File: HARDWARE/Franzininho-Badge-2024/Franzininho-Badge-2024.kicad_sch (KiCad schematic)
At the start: 47 parts, among them J1 Conn_01x03_Pin, J2 Conn_01x04_Pin, Q1 SIL2308, SW1 ON/OFF, SW2 USER, SW3 RESET, U1 1.54in 200x200, U2 CH32V003F4P6, U3 2.13in 250x122, U4 OLED 128x64 1.3"

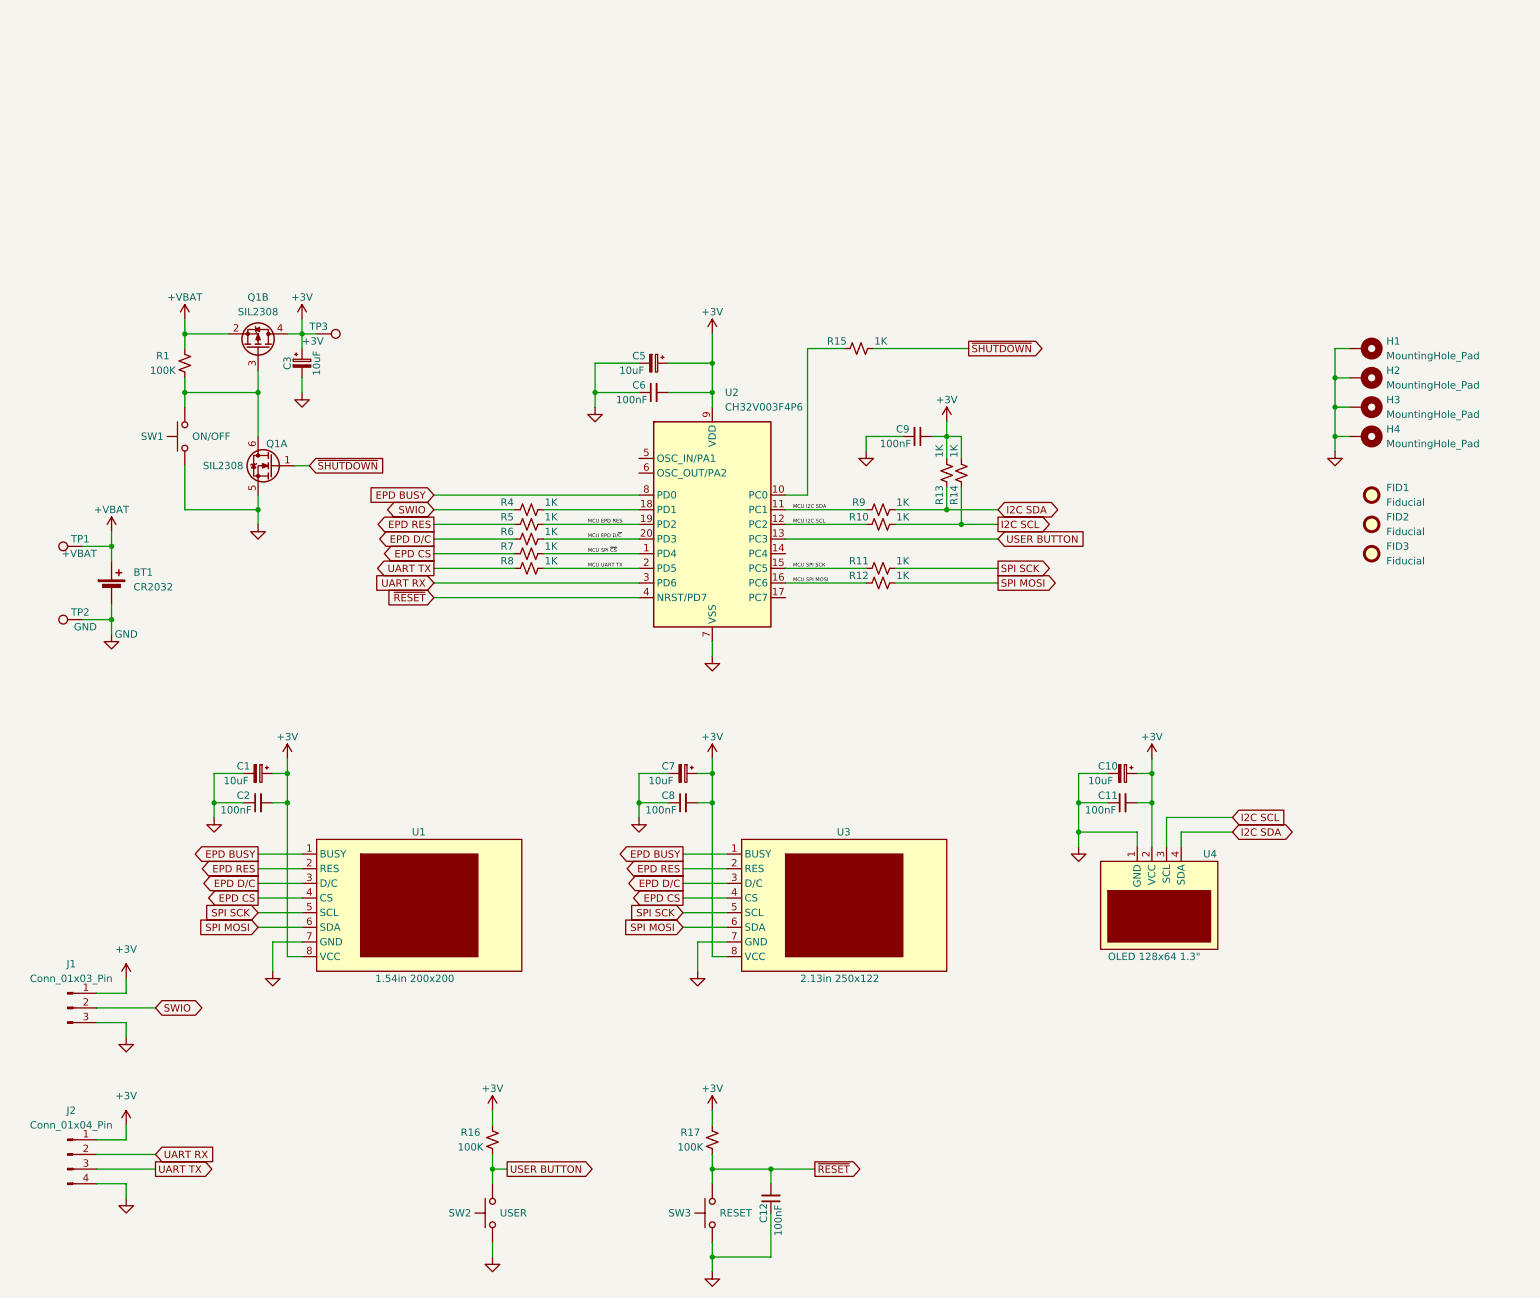
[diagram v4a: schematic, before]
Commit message: Finalização do projeto; adicionados test points e LEDs; adicionado conector para SPI; ajuste nas marcações; renumeração; ajustes no layout.
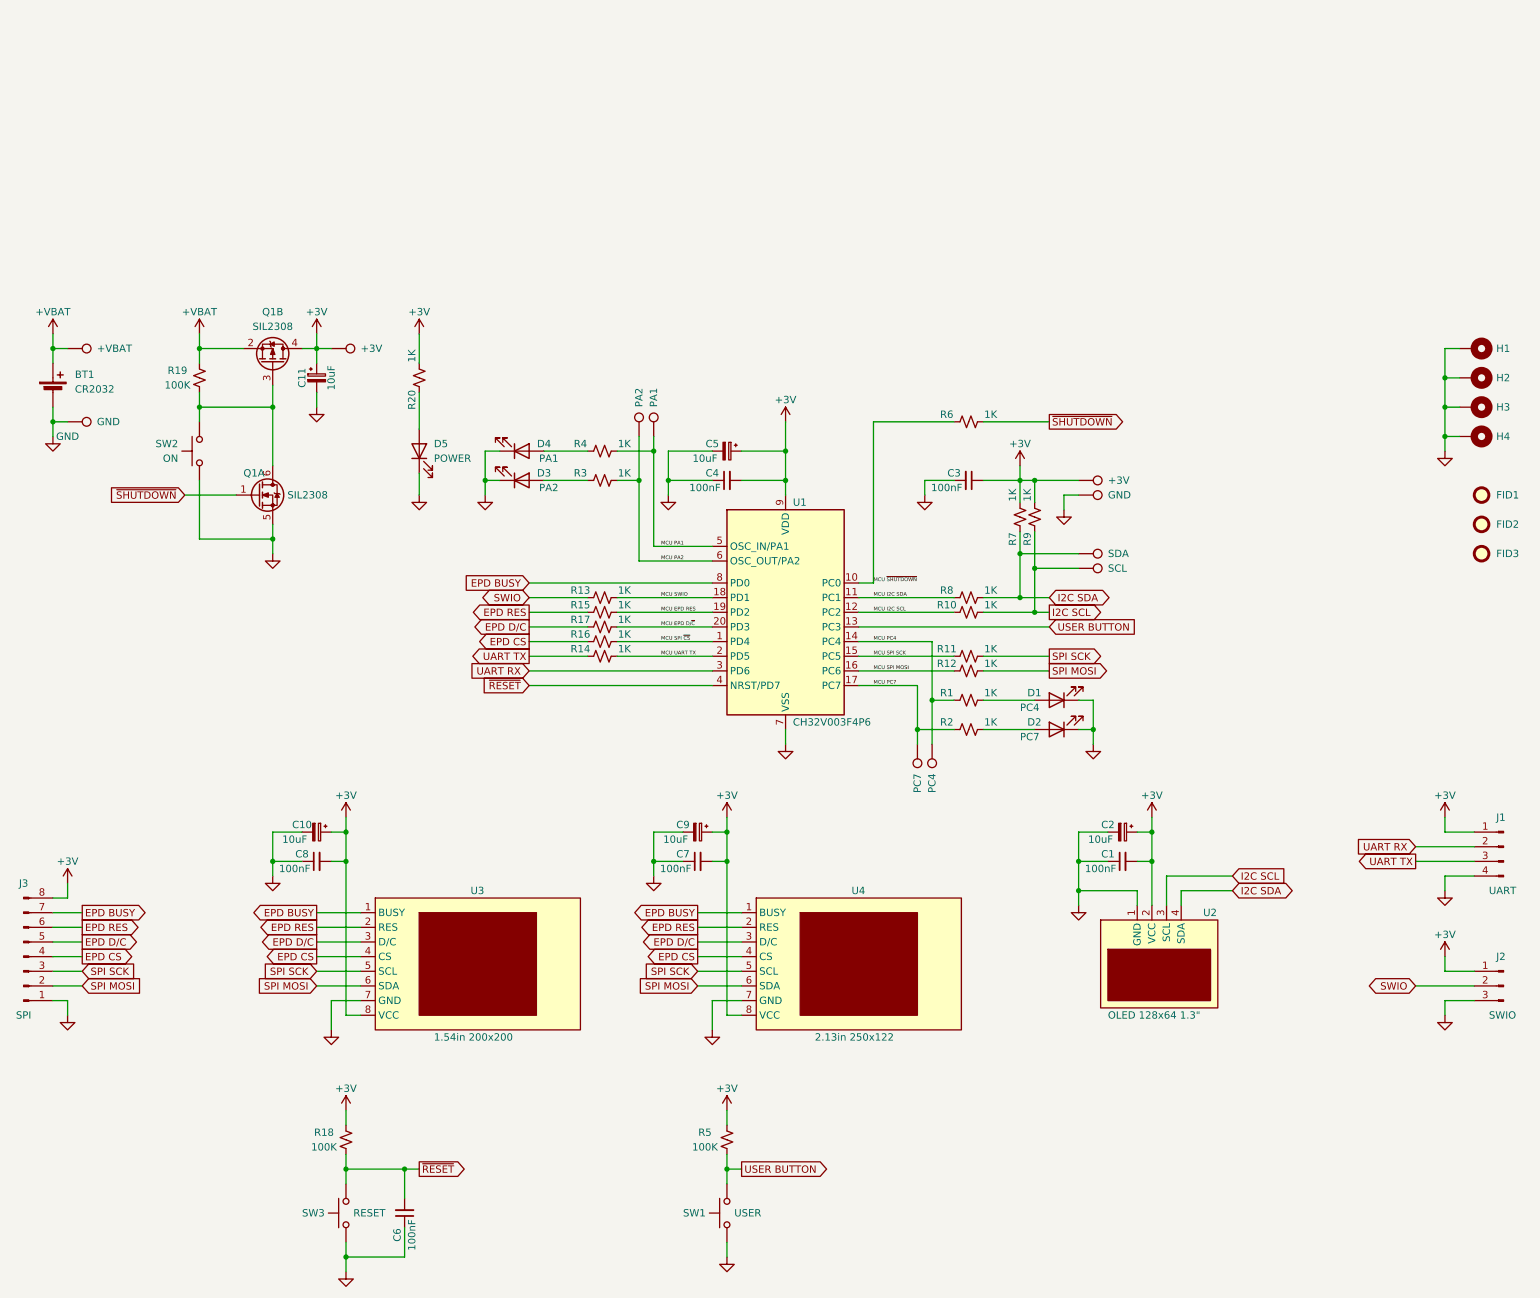
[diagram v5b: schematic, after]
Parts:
- added D1: PC4, LED_SMD:LED_0603_1608Metric_Pad1.05x0.95mm_HandSolder, symbol Device:LED
- added D2: PC7, LED_SMD:LED_0603_1608Metric_Pad1.05x0.95mm_HandSolder, symbol Device:LED
- added D3: PA2, LED_SMD:LED_0603_1608Metric_Pad1.05x0.95mm_HandSolder, symbol Device:LED
- added D4: PA1, LED_SMD:LED_0603_1608Metric_Pad1.05x0.95mm_HandSolder, symbol Device:LED
- added D5: POWER, LED_SMD:LED_0603_1608Metric_Pad1.05x0.95mm_HandSolder, symbol Device:LED
- added J3: SPI, Connector_PinHeader_2.54mm:PinHeader_1x08_P2.54mm_Horizontal, symbol Connector:Conn_01x08_Pin
- added R1, R2, R20, R3, R4: 1K, Resistor_SMD:R_0603_1608Metric_Pad0.98x0.95mm_HandSolder, symbol Device:R_Small_US
- added TP1: SDA, TestPoint:TestPoint_THTPad_D1.5mm_Drill0.7mm, symbol Connector:TestPoint
- added TP2: SCL, TestPoint:TestPoint_THTPad_D1.5mm_Drill0.7mm, symbol Connector:TestPoint
- added TP3: +3V, TestPoint:TestPoint_THTPad_D1.5mm_Drill0.7mm, symbol Connector:TestPoint
- added TP4: GND, TestPoint:TestPoint_THTPad_D1.5mm_Drill0.7mm, symbol Connector:TestPoint
- added TP5: PC4, TestPoint:TestPoint_THTPad_D1.5mm_Drill0.7mm, symbol Connector:TestPoint
- added TP6: PC7, TestPoint:TestPoint_THTPad_D1.5mm_Drill0.7mm, symbol Connector:TestPoint
- added TP7: PA2, TestPoint:TestPoint_THTPad_D1.5mm_Drill0.7mm, symbol Connector:TestPoint
- added TP8: PA1, TestPoint:TestPoint_THTPad_D1.5mm_Drill0.7mm, symbol Connector:TestPoint
- J1: renamed from J2; value Conn_01x04_Pin -> UART
- J2: renamed from J1; value Conn_01x03_Pin -> SWIO
- SW2: renamed from SW1; value ON/OFF -> ON
- renumbered C11 to C1, C1 to C10, C3 to C11, C10 to C2, C9 to C3, C6 to C4, C12 to C6, C8 to C7, C2 to C8, C7 to C9, R4 to R13, R8 to R14, R5 to R15, R7 to R16, R6 to R17, R17 to R18, R1 to R19, R16 to R5, R15 to R6, R13 to R7, R9 to R8, R14 to R9, SW2 to SW1, TP1 to TP10, TP3 to TP11, TP2 to TP9, U2 to U1, U4 to U2, U1 to U3, U3 to U4
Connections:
- net +3V: now also J3.8 (Pin_8), R20.2, TP3.1
- net EPD BUSY: now also J3.7 (Pin_7)
- net EPD CS: now also J3.4 (Pin_4)
- net EPD D/C: now also J3.5 (Pin_5)
- net EPD RES: now also J3.6 (Pin_6)
- net GND: now also D1.1 (K), D2.1 (K), D3.1 (K), D4.1 (K), D5.1 (K), J3.1 (Pin_1), TP4.1
- net I2C SCL: now also TP2.1
- net I2C SDA: now also TP1.1
- net SPI MOSI: now also J3.2 (Pin_2)
- net SPI SCK: now also J3.3 (Pin_3)
- net MCU SWIO: now reaches R13.2, U1.18 (PD1)
- net MCU ~{SHUTDOWN}: now reaches R6.1, U1.10 (PC0)
- net MCU PC4: now reaches U1.14 (PC4)
- net MCU PC4: now also R1.1, TP5.1
- net MCU PC7: now reaches U1.17 (PC7)
- net MCU PC7: now also R2.1, TP6.1
- net MCU PA1: now reaches U1.5 (OSC_IN/PA1)
- net MCU PA1: now also R4.2, TP8.1
- net MCU PA2: now reaches U1.6 (OSC_OUT/PA2)
- net MCU PA2: now also R3.2, TP7.1
- new net: D1.2 (A), R1.2
- new net: D2.2 (A), R2.2
- new net: D5.2 (A), R20.1
- new net: D4.2 (A), R4.1
- new net: D3.2 (A), R3.1
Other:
- company: (none) -> Eng. André A. M. Araújo
- moved on the sheet: BT1, C1, C10, C11, C2, C3, C4, C5, C6, C7, C8, C9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

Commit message: Finalização do esquemático e layout.
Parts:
- U3: value 1.54in 200x200 -> EPD 200x200 1.54"
- U4: value 2.13in 250x122 -> EPD 250x122 2.13"
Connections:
- net LED PC4: now reaches D1.2 (A), R1.2
- net LED PC7: now reaches D2.2 (A), R2.2
- net LED POWER: now reaches D5.2 (A), R20.1
- net SWITCH ~{ON}: now reaches Q1.3 (G2), Q1.6 (D1), R19.1, SW2.2
- net LED PA1: now reaches D4.2 (A), R4.1
- net LED PA2: now reaches D3.2 (A), R3.1
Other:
- moved on the sheet: D1, D2, D3, D4, D5, R20

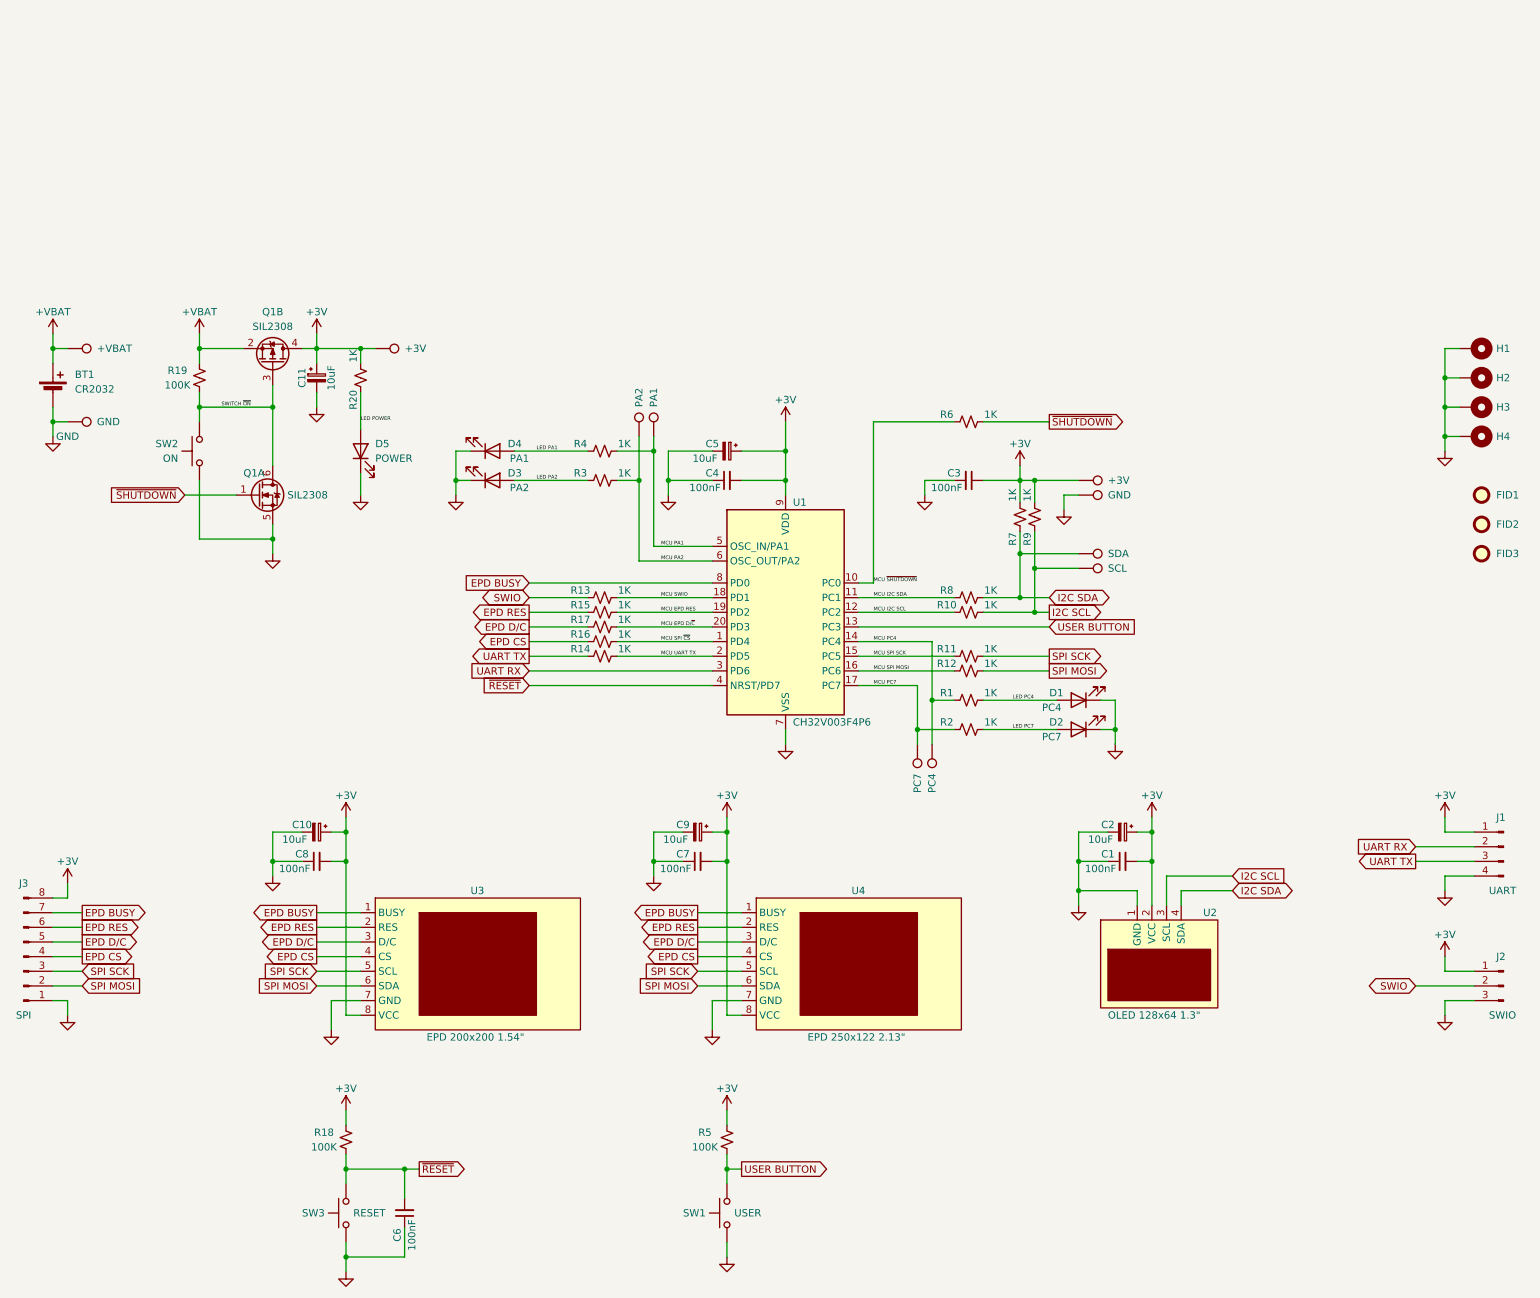
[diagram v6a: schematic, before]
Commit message: Revisão de valores dos resistores. Geração de novo PDF do esquemático.
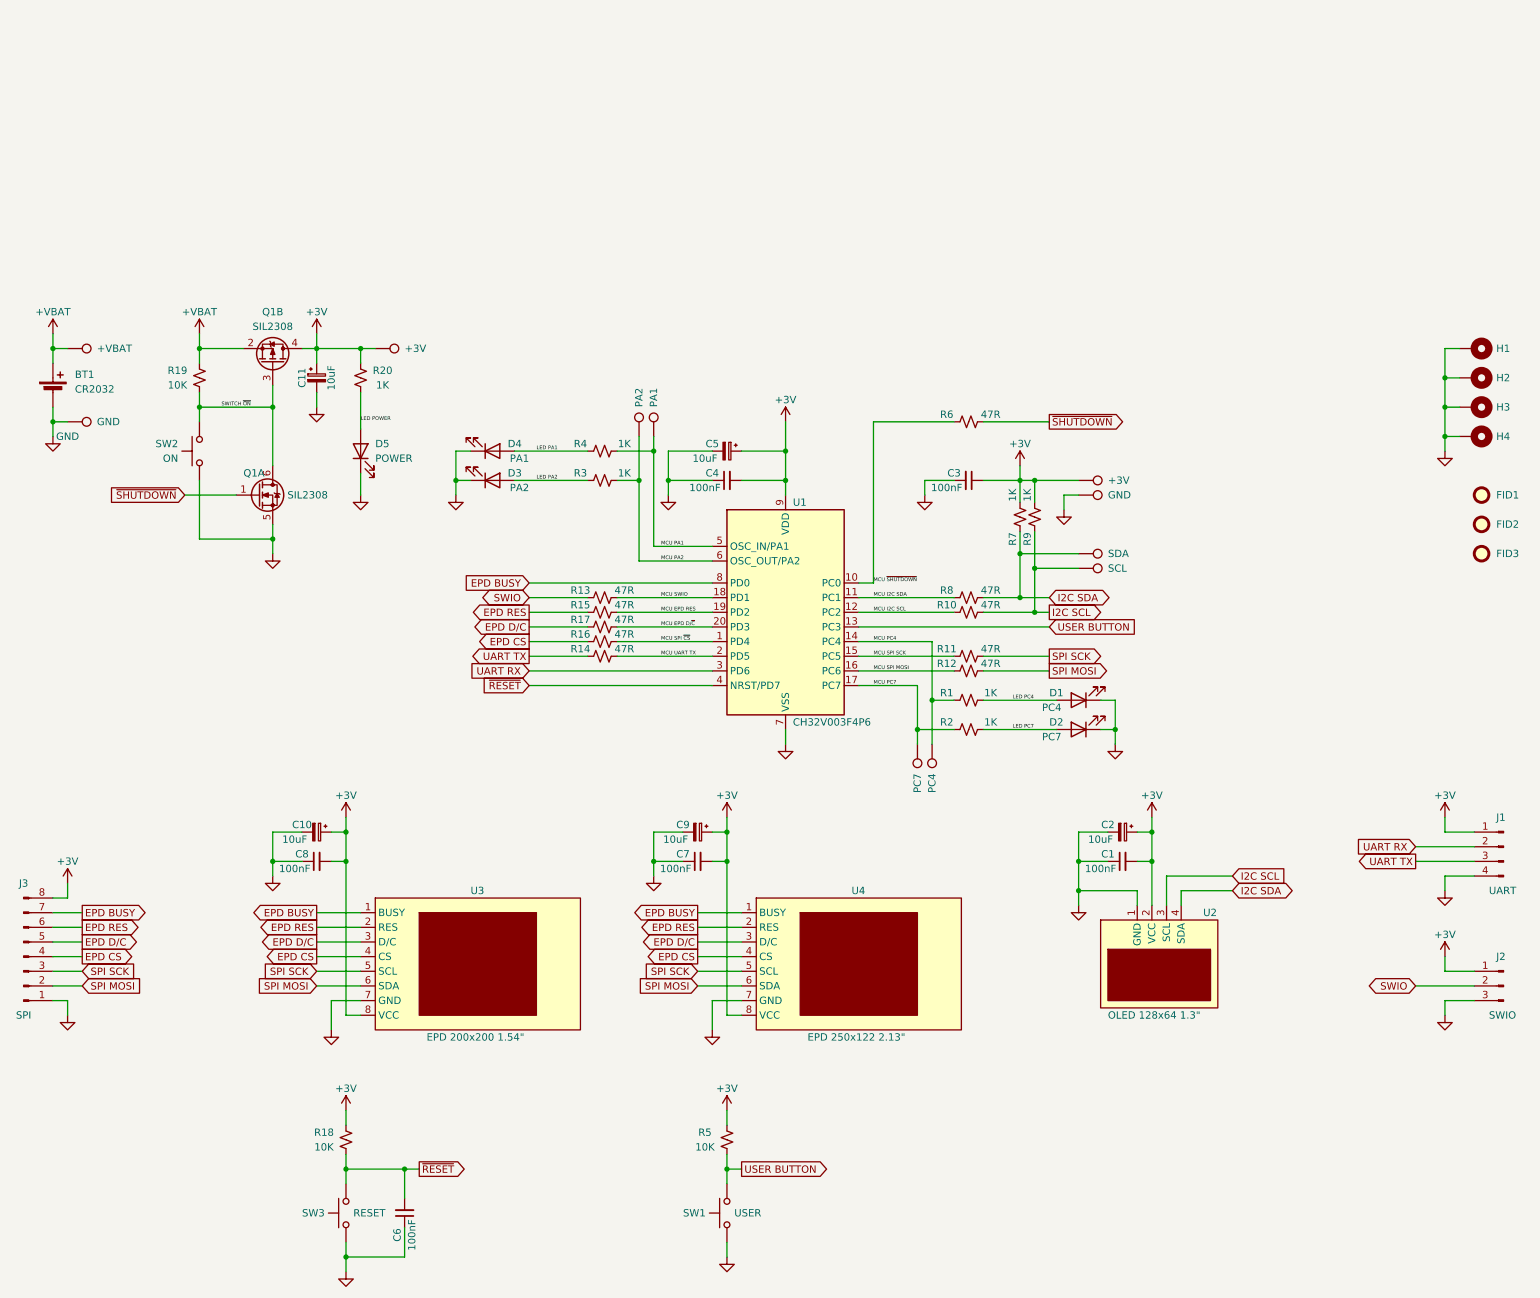
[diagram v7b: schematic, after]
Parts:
- R10, R11, R12, R13, R14, R15, R16, R17, R6, R8: value 1K -> 47R
- R18, R19, R5: value 100K -> 10K
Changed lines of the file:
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@@
 			)
 		)
-		(property "Value" "1K"
+		(property "Value" "47R"
 			(at 124.46 67.31 90)
 			(effects
@@
 			)
 		)
-		(property "Value" "1K"
+		(property "Value" "47R"
 			(at 187.96 69.85 90)
 			(effects
@@
 			)
 		)
-		(property "Value" "1K"
+		(property "Value" "47R"
 			(at 124.46 77.47 90)
 			(effects
@@
 			)
 		)
-		(property "Value" "1K"
+		(property "Value" "47R"
 			(at 187.96 36.83 90)
 			(effects
@@
 			)
 		)
-		(property "Value" "100K"
+		(property "Value" "10K"
 			(at 138.43 163.83 0)
 			(effects
@@
 			)
 		)
-		(property "Value" "100K"
+		(property "Value" "10K"
 			(at 72.39 163.83 0)
 			(effects
@@
 			)
 		)
-		(property "Value" "1K"
+		(property "Value" "47R"
 			(at 187.96 80.01 90)
 			(effects
@@
 			)
 		)
-		(property "Value" "1K"
+		(property "Value" "47R"
 			(at 124.46 72.39 90)
 			(effects
@@
 		(dnp no)
 		(property "Reference" "R20"
-			(at 77.47 34.29 90)
+			(at 82.55 29.21 0)
 			(effects
 				(font
@@
 		)
 		(property "Value" "1K"
-			(at 77.47 26.67 90)
+			(at 82.55 31.75 0)
 			(effects
 				(font
@@
 			)
 		)
-		(property "Value" "1K"
+		(property "Value" "47R"
 			(at 187.96 77.47 90)
 			(effects
@@
 			)
 		)
-		(property "Value" "100K"
+		(property "Value" "10K"
 			(at 46.99 31.75 0)
 			(effects
@@
 			)
 		)
-		(property "Value" "1K"
+		(property "Value" "47R"
 			(at 187.96 67.31 90)
 			(effects
@@
 			)
 		)
-		(property "Value" "1K"
+		(property "Value" "47R"
 			(at 124.46 69.85 90)
 			(effects
@@
 			)
 		)
-		(property "Value" "1K"
+		(property "Value" "47R"
 			(at 124.46 74.93 90)
 			(effects
